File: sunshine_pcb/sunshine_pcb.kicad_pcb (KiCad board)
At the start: 2 copper layers, 82.5 x 61.9 mm, 17 parts, among them J1 XT30PW, J2 XT30PW, J3 MR30, J4 MR30, J5 USB_C_Receptacle_USB2.0_16P, SW1 Fingertech, U1 RP2350_60QFN, U2 W25Q128JVP, U3 LIS3MDL, U4 ADXL375, U5 HT7533, U6 FS2A, U7 DualAM32

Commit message: Do layout
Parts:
- added C10: 100nF, PCM_JLCPCB:C_0402, B.Cu at (104.0, 118.0)
- added C11: 100nF, PCM_JLCPCB:C_0402, B.Cu at (115.5, 116.7)
- added C12: 4.7uF, PCM_JLCPCB:C_0402, B.Cu at (109.8, 112.2)
- added C13: 100nF, PCM_JLCPCB:C_0402, B.Cu at (115.5, 120.2)
- added C14: 100nF, PCM_JLCPCB:C_0402, B.Cu at (115.5, 115.8)
- added C15: 100nF, PCM_JLCPCB:C_0402, B.Cu at (112.4, 112.2)
- added C16: 100nF, PCM_JLCPCB:C_0402, B.Cu at (108.1, 112.0)
- added C17: 100nF, PCM_JLCPCB:C_0402, B.Cu at (104.0, 116.0)
- added C18: 100nF, PCM_JLCPCB:C_0402, B.Cu at (103.9, 120.5)
- added C19: 100nF, PCM_JLCPCB:C_0402, B.Cu at (107.7, 124.2)
- added C22: 100nF, PCM_JLCPCB:C_0402, F.Cu at (112.4, 124.4)
- added C23: 15pF, PCM_JLCPCB:C_0402, B.Cu at (105.2, 109.5)
- added C24: 15pF, PCM_JLCPCB:C_0402, B.Cu at (108.2, 105.8)
- added C25: 100nF, PCM_JLCPCB:C_0402, F.Cu at (102.5, 113.3)
- added C26: 100nF, PCM_JLCPCB:C_0402, F.Cu at (98.0, 114.0)
- added C27: 100nF, PCM_JLCPCB:C_0402, F.Cu at (108.4, 109.5)
- added C28: 100nF, PCM_JLCPCB:C_0402, F.Cu at (109.8, 109.0)
- added C29: 4.7uF, PCM_JLCPCB:C_0402, F.Cu at (109.8, 109.8)
- added C3: 10u, Capacitor_SMD:C_1210_3225Metric, F.Cu at (94.8, 93.8)
- added C30: 100nF, PCM_JLCPCB:C_0402, B.Cu at (115.5, 117.5)
- added C4: 10u, Capacitor_SMD:C_1210_3225Metric, F.Cu at (101.4, 93.8)
- added C5: 10uF, PCM_JLCPCB:C_0805, F.Cu at (89.3, 126.4)
- added C6: 10uF, PCM_JLCPCB:C_0805, F.Cu at (86.2, 122.0)
- added C7: 4.7uF, PCM_JLCPCB:C_0402, B.Cu at (113.3, 123.0)
- added C8: 4.7uF, PCM_JLCPCB:C_0402, B.Cu at (111.4, 122.2)
- added C9: 4.7uF, PCM_JLCPCB:C_0402, B.Cu at (111.4, 123.0)
- added D2: 1N5819WS, PCM_JLCPCB:D_SOD-323, F.Cu at (106.6, 93.2)
- added D3: 1N5819WS, PCM_JLCPCB:D_SOD-323, F.Cu at (101.5, 117.3)
- added D4: LED, LED_SMD:LED_PLCC_2835, B.Cu at (100.0, 122.0)
- added D5: LED, LED_SMD:LED_PLCC_2835, B.Cu at (100.0, 112.8)
- added D6: LED, LED_SMD:LED_PLCC_2835, B.Cu at (100.0, 117.4)
- added D7: SMF12A, PCM_JLCPCB:D_SOD-123FL, F.Cu at (104.3, 93.8)
- added Q1: AO3401A, PCM_JLCPCB:Q_SOT-23, F.Cu at (93.7, 126.9)
- added R1: 5.1kΩ, PCM_JLCPCB:R_0402, F.Cu at (99.2, 117.3)
- added R10: 33Ω, PCM_JLCPCB:R_0805, F.Cu at (91.5, 123.3)
- added R11: 1kΩ, PCM_JLCPCB:R_0402, F.Cu at (94.5, 123.6)
- added R12: 33Ω, PCM_JLCPCB:R_0805, F.Cu at (91.5, 121.3)
- added R13: 33Ω, PCM_JLCPCB:R_0805, F.Cu at (91.5, 117.3)
- added R14: 33Ω, PCM_JLCPCB:R_0805, F.Cu at (91.5, 119.3)
- added R15: 5.1kΩ, PCM_JLCPCB:R_0402, B.Cu at (115.5, 119.3)
- added R16: 5.1kΩ, PCM_JLCPCB:R_0402, B.Cu at (117.4, 119.3)
- added R17: 5.1kΩ, PCM_JLCPCB:R_0402, B.Cu at (115.5, 118.5)
- added R18: 1kΩ, PCM_JLCPCB:R_0402, B.Cu at (117.4, 118.5)
- added R19: 5.1kΩ, PCM_JLCPCB:R_0402, F.Cu at (94.5, 124.5)
- added R2: 5.1kΩ, PCM_JLCPCB:R_0402, F.Cu at (100.5, 125.0)
- added R3: 5.1kΩ, PCM_JLCPCB:R_0402, F.Cu at (96.2, 117.8)
- added R4: 33Ω, PCM_JLCPCB:R_0402, B.Cu at (113.3, 122.2)
- added R5: 33Ω, PCM_JLCPCB:R_0402, B.Cu at (108.6, 124.2)
- added R6: 33Ω, PCM_JLCPCB:R_0402, B.Cu at (109.5, 124.2)
- added R7: 1kΩ, PCM_JLCPCB:R_0402, B.Cu at (93.8, 117.3)
- added R8: 1kΩ, PCM_JLCPCB:R_0402, B.Cu at (109.8, 107.2)
- added R9: 1kΩ, PCM_JLCPCB:R_0402, F.Cu at (114.5, 115.8)
- added S1: TS-1187A-C-B-B, PCM_JLCPCB:SW-SMD_4P-L5.1-W5.1-P3.70-LS6.5-TL-2, B.Cu at (90.1, 120.2)
- added S2: TS-1187A-C-B-B, PCM_JLCPCB:SW-SMD_4P-L5.1-W5.1-P3.70-LS6.5-TL-2, F.Cu at (109.5, 117.2)
- added U8: USBLC6-2P6, Package_TO_SOT_SMD:SOT-666, F.Cu at (100.3, 126.6)
- added Y1: ABM8-272-T3, Crystal:Crystal_SMD_3225-4Pin_3.2x2.5mm, B.Cu at (107.5, 108.3)
- D1: moved to B.Cu
- J1, J2: value XT30PW -> Soldered; footprint Connector_AMASS:AMASS_XT30PW-M_1x02_P2.50mm_Horizontal -> Connector_Wire:SolderWire-0.5sqmm_1x02_P4.6mm_D0.9mm_OD2.1mm_Relief
- J3, J4: value MR30 -> Soldered; footprint Connector_AMASS:AMASS_MR30PW-M_1x03_P3.50mm_Horizontal -> Connector_Wire:SolderWire-0.5sqmm_1x03_P4.6mm_D0.9mm_OD2.1mm_Relief
- J5: value USB_C_Receptacle_USB2.0_16P -> VerticalUSB
- L1: value L -> 3.3u; moved to B.Cu
- U1: footprint Package_DFN_QFN:QFN-60-1EP_7x7mm_P0.4mm_EP3.4x3.4mm -> Package_DFN_QFN:QFN-60-1EP_7x7mm_P0.4mm_EP3.4x3.4mm_ThermalVias; moved to B.Cu
- moved L1 78.1 mm to (111.4, 124.5)
- moved U5 77.1 mm to (85.8, 125.5)
- moved U3 66.7 mm to (109.4, 107.2)
- moved U2 66.1 mm to (108.5, 125.9)
- moved U1 66.0 mm to (109.4, 117.3)
- moved U4 65.2 mm to (100.0, 111.0), turned to 90 degrees
- moved J1 62.7 mm to (79.0, 114.0), turned to -30 degrees
- moved C1 60.4 mm to (88.4, 94.5)
- moved C2 58.6 mm to (98.1, 93.8), turned to 90 degrees
- moved J2 50.8 mm to (121.0, 86.0), turned to 150 degrees
- moved SW1 49.3 mm to (100.0, 100.0), turned to 0 degrees
- moved J4 47.2 mm to (118.0, 113.5)
- moved U6 46.4 mm to (90.0, 108.2), turned to -90 degrees
- moved J5 43.3 mm to (100.0, 121.4)
- moved D1 36.2 mm to (100.0, 126.6), turned to -90 degrees
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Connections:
- net Net-(J5-VBUS-PadA4) renamed VBUS
- C1 pad 1: unconnected-(C1-Pad1) -> VDC
- C1 pad 2: unconnected-(C1-Pad2) -> GND
- C2 pad 1: unconnected-(C2-Pad1) -> VDC
- C2 pad 2: unconnected-(C2-Pad2) -> GND
- D1 pad 1: unconnected-(D1-K-Pad1) -> GND
- D1 pad 2: unconnected-(D1-A-Pad2) -> Net-(D1-A)
- J1 pad 1: unconnected-(J1---Pad1) -> /BATT1_+
- J1 pad 2: unconnected-(J1-+-Pad2) -> /BATT2_+
- J2 pad 1: unconnected-(J2---Pad1) -> /BATT2_+
- J2 pad 2: unconnected-(J2-+-Pad2) -> GND
- J3 pad 1: unconnected-(J3-Pin_1-Pad1) -> Net-(J3-Pin_1)
- J3 pad 2: unconnected-(J3-Pin_2-Pad2) -> Net-(J3-Pin_2)
- J3 pad 3: unconnected-(J3-Pin_3-Pad3) -> Net-(J3-Pin_3)
- J4 pad 1: unconnected-(J4-Pin_1-Pad1) -> Net-(J4-Pin_1)
- J4 pad 2: unconnected-(J4-Pin_2-Pad2) -> Net-(J4-Pin_2)
- J4 pad 3: unconnected-(J4-Pin_3-Pad3) -> Net-(J4-Pin_3)
- J5 pad A1: Net-(J5-GND-PadA1) -> GND
- J5 pad A12: Net-(J5-GND-PadA1) -> GND
- J5 pad A5: unconnected-(J5-CC1-PadA5) -> Net-(J5-CC1)
- J5 pad A6: unconnected-(J5-D+-PadA6) -> /USB_C_D+
- J5 pad A7: unconnected-(J5-D--PadA7) -> /USB_C_D-
- J5 pad B1: Net-(J5-GND-PadA1) -> GND
- J5 pad B12: Net-(J5-GND-PadA1) -> GND
- J5 pad B5: unconnected-(J5-CC2-PadB5) -> Net-(J5-CC2)
- J5 pad B6: unconnected-(J5-D+-PadB6) -> /USB_C_D+
- J5 pad B7: unconnected-(J5-D--PadB7) -> /USB_C_D-
- J5 pad S1: unconnected-(J5-SHIELD-PadS1) -> Net-(J5-SHIELD)
- L1 pad 1: unconnected-(L1-Pad1) -> +1V1
- L1 pad 2: unconnected-(L1-Pad2) -> /VREG_LX
- SW1 pad 1: unconnected-(SW1-A-Pad1) -> /BATT1_+
- SW1 pad 2: unconnected-(SW1-B-Pad2) -> VDC
- U1 pad 1: unconnected-(U1-IOVDD-Pad1) -> +3V3
- U1 pad 10: unconnected-(U1-GPIO7-Pad10) -> /R4
- U1 pad 11: unconnected-(U1-IOVDD-Pad11) -> +3V3
- U1 pad 12: unconnected-(U1-GPIO8-Pad12) -> /S2
- U1 pad 13: unconnected-(U1-GPIO9-Pad13) -> /LED
- U1 pad 14: unconnected-(U1-GPIO10-Pad14) -> /IMU_SCK
- U1 pad 15: unconnected-(U1-GPIO11-Pad15) -> /IMU_MOSI
- U1 pad 16: unconnected-(U1-GPIO12-Pad16) -> /IMU_MISO
- U1 pad 17: unconnected-(U1-GPIO13-Pad17) -> /IMU_CS
- U1 pad 18: unconnected-(U1-GPIO14-Pad18) -> /IMU_INT1
- U1 pad 19: unconnected-(U1-GPIO15-Pad19) -> /IMU_INT2
- U1 pad 20: unconnected-(U1-IOVDD-Pad20) -> +3V3
- U1 pad 21: unconnected-(U1-XIN-Pad21) -> Net-(U1-XIN)
- U1 pad 22: unconnected-(U1-XOUT-Pad22) -> Net-(U1-XOUT)
- U1 pad 23: unconnected-(U1-DVDD-Pad23) -> +1V1
- U1 pad 26: unconnected-(U1-RUN-Pad26) -> /RESET
- U1 pad 27: unconnected-(U1-GPIO16-Pad27) -> /MAG_MISO
- U1 pad 28: unconnected-(U1-GPIO17-Pad28) -> /MAG_CS
- U1 pad 29: unconnected-(U1-GPIO18-Pad29) -> /MAG_SCK
- U1 pad 3: unconnected-(U1-GPIO1-Pad3) -> /R1
- U1 pad 30: unconnected-(U1-IOVDD-Pad30) -> +3V3
- U1 pad 31: unconnected-(U1-GPIO19-Pad31) -> /MAG_MOSI
- U1 pad 32: unconnected-(U1-GPIO20-Pad32) -> /MAG_DRDY
- U1 pad 33: unconnected-(U1-GPIO21-Pad33) -> /MAG_INT
- U1 pad 38: unconnected-(U1-IOVDD-Pad38) -> +3V3
- U1 pad 39: unconnected-(U1-DVDD-Pad39) -> +1V1
- U1 pad 40: unconnected-(U1-GPIO26_ADC0-Pad40) -> Net-(U1-GPIO26_ADC0)
- U1 pad 44: unconnected-(U1-ADC_AVDD-Pad44) -> +3V3
- U1 pad 45: unconnected-(U1-IOVDD-Pad45) -> +3V3
- U1 pad 46: unconnected-(U1-VREG_AVDD-Pad46) -> /VREG_AVDD
- U1 pad 47: unconnected-(U1-VREG_PGND-Pad47) -> GND
- U1 pad 48: unconnected-(U1-VREG_LX-Pad48) -> /VREG_LX
- U1 pad 49: unconnected-(U1-VREG_VIN-Pad49) -> +3V3
- U1 pad 5: unconnected-(U1-GPIO3-Pad5) -> /R2
- U1 pad 50: unconnected-(U1-VREG_FB-Pad50) -> +1V1
- U1 pad 51: unconnected-(U1-USB_DM-Pad51) -> Net-(U1-USB_DM)
- U1 pad 52: unconnected-(U1-USB_DP-Pad52) -> Net-(U1-USB_DP)
- U1 pad 53: unconnected-(U1-USB_OTP_VDD-Pad53) -> +3V3
- U1 pad 54: unconnected-(U1-QSPI_IOVDD-Pad54) -> +3V3
- U1 pad 55: unconnected-(U1-QSPI_SD3-Pad55) -> /QSPI_SD3
- U1 pad 56: unconnected-(U1-QSPI_SCLK-Pad56) -> /QSPI_SCK
- U1 pad 57: unconnected-(U1-QSPI_SD0-Pad57) -> /QSPI_SD0
- U1 pad 58: unconnected-(U1-QSPI_SD2-Pad58) -> /QSPI_SD2
- U1 pad 59: unconnected-(U1-QSPI_SD1-Pad59) -> /QSPI_SD1
- U1 pad 6: unconnected-(U1-DVDD-Pad6) -> +1V1
- U1 pad 60: unconnected-(U1-QSPI_SS-Pad60) -> /QSPI_SS
- U1 pad 61: unconnected-(U1-GND-Pad61) -> GND
- U1 pad 8: unconnected-(U1-GPIO5-Pad8) -> /R3
- U1 pad 9: unconnected-(U1-GPIO6-Pad9) -> /S1
- U2 pad 1: unconnected-(U2-~{CS}-Pad1) -> /QSPI_SS
- U2 pad 2: unconnected-(U2-DO/IO_{1}-Pad2) -> /QSPI_SD1
- U2 pad 3: unconnected-(U2-~{WP}/IO_{2}-Pad3) -> /QSPI_SD2
- U2 pad 4: unconnected-(U2-GND-Pad4) -> GND
- U2 pad 5: unconnected-(U2-DI/IO_{0}-Pad5) -> /QSPI_SD0
- U2 pad 6: unconnected-(U2-CLK-Pad6) -> /QSPI_SCK
- U2 pad 7: unconnected-(U2-~{HOLD}/~{RESET}/IO_{3}-Pad7) -> /QSPI_SD3
- U2 pad 8: unconnected-(U2-VCC-Pad8) -> +3V3
- U2 pad 9: unconnected-(U2-EP-Pad9) -> GND
- U3 pad 1: unconnected-(U3-SCL/SPC-Pad1) -> /MAG_SCK
- U3 pad 10: unconnected-(U3-~{CS}-Pad10) -> /MAG_CS
- U3 pad 11: unconnected-(U3-SDA/SDI/SDO-Pad11) -> /MAG_MOSI
- U3 pad 12: Net-(U3-GND-Pad12) -> GND
- U3 pad 2: Net-(U3-GND-Pad12) -> GND
- U3 pad 3: Net-(U3-GND-Pad12) -> GND
- U3 pad 4: unconnected-(U3-C1-Pad4) -> Net-(U3-C1)
- U3 pad 5: unconnected-(U3-Vdd-Pad5) -> +3V3
- U3 pad 6: unconnected-(U3-Vdd_IO-Pad6) -> +3V3
- U3 pad 7: unconnected-(U3-INT-Pad7) -> /MAG_INT
- U3 pad 8: unconnected-(U3-DRDY-Pad8) -> /MAG_DRDY
- U3 pad 9: unconnected-(U3-SDO/SA1-Pad9) -> /MAG_MISO
- U4 pad 1: unconnected-(U4-Vdd_I/O-Pad1) -> +3V3
- U4 pad 12: unconnected-(U4-SDO/ADDR-Pad12) -> /IMU_MISO
- U4 pad 13: unconnected-(U4-SDA/SDI/SDIO-Pad13) -> /IMU_MOSI
- U4 pad 14: unconnected-(U4-SCL/SCLK-Pad14) -> /IMU_SCK
- U4 pad 2: Net-(U4-GND-Pad2) -> GND
- U4 pad 4: Net-(U4-GND-Pad2) -> GND
- U4 pad 5: Net-(U4-GND-Pad2) -> GND
- U4 pad 6: unconnected-(U4-Vs-Pad6) -> +3V3
- U4 pad 7: unconnected-(U4-~{CS}-Pad7) -> /IMU_CS
- U4 pad 8: unconnected-(U4-INT1-Pad8) -> /IMU_INT1
- U4 pad 9: unconnected-(U4-INT2-Pad9) -> /IMU_INT2
- U5 pad 1: unconnected-(U5-GND-Pad1) -> GND
- U5 pad 2: unconnected-(U5-VIN-Pad2) -> +5V
- U5 pad 3: unconnected-(U5-VOUT-Pad3) -> +3V3
- U6 pad 1: unconnected-(U6-Pad1) -> /R1
- U6 pad 2: unconnected-(U6-Pad2) -> /R2
- U6 pad 3: unconnected-(U6-Pad3) -> /R3
- U6 pad 4: unconnected-(U6-Pad4) -> /R4
- U6 pad 5: unconnected-(U6-+5V-Pad5) -> +5V
- U6 pad 6: unconnected-(U6-GND-Pad6) -> GND
- U7 pad 1: unconnected-(U7-M1A-Pad1) -> Net-(J3-Pin_3)
- U7 pad 10: unconnected-(U7-S2-Pad10) -> /S2
- U7 pad 11: unconnected-(U7-+5V-Pad11) -> Net-(U7-+5V)
- U7 pad 12: Net-(U7-GND-Pad12) -> GND
- U7 pad 2: unconnected-(U7-M1B-Pad2) -> Net-(J3-Pin_2)
- U7 pad 3: unconnected-(U7-M1C-Pad3) -> Net-(J3-Pin_1)
- U7 pad 4: unconnected-(U7-M2A-Pad4) -> Net-(J4-Pin_1)
- U7 pad 5: unconnected-(U7-M2B-Pad5) -> Net-(J4-Pin_2)
- U7 pad 6: unconnected-(U7-M2C-Pad6) -> Net-(J4-Pin_3)
- U7 pad 7: unconnected-(U7-+VDC-Pad7) -> VDC
- U7 pad 8: Net-(U7-GND-Pad12) -> GND
- U7 pad 9: unconnected-(U7-S1-Pad9) -> /S1
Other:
- board size 82.5 x 61.9 mm -> 59 x 58 mm
- board text added: "+"

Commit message: Add some protection
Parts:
- added D10: SMF5.0A, PCM_JLCPCB:D_SOD-123FL, F.Cu at (113.5, 93.7)
- added D8: SMF5.0A, PCM_JLCPCB:D_SOD-123FL, F.Cu at (108.7, 93.7)
- added D9: SMF5.0A, PCM_JLCPCB:D_SOD-123FL, F.Cu at (111.1, 93.7)
- added R20: 1kΩ, PCM_JLCPCB:R_0402, F.Cu at (106.5, 95.1)
- added R21: 1kΩ, PCM_JLCPCB:R_0402, F.Cu at (106.5, 96.0)
- J1, J2: footprint Connector_Wire:SolderWire-0.5sqmm_1x02_P4.6mm_D0.9mm_OD2.1mm_Relief -> Connector_Wire:SolderWire-0.75sqmm_1x02_P4.8mm_D1.25mm_OD2.3mm_Relief
- moved J1 1.58 mm to (79.5, 112.5)
- moved J2 1.58 mm to (120.5, 87.5)
- moved D2 0.22 mm to (106.5, 93.0), turned to 90 degrees
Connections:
- U7 pad 10: /S2 -> /S2_C
- U7 pad 9: /S1 -> /S1_C

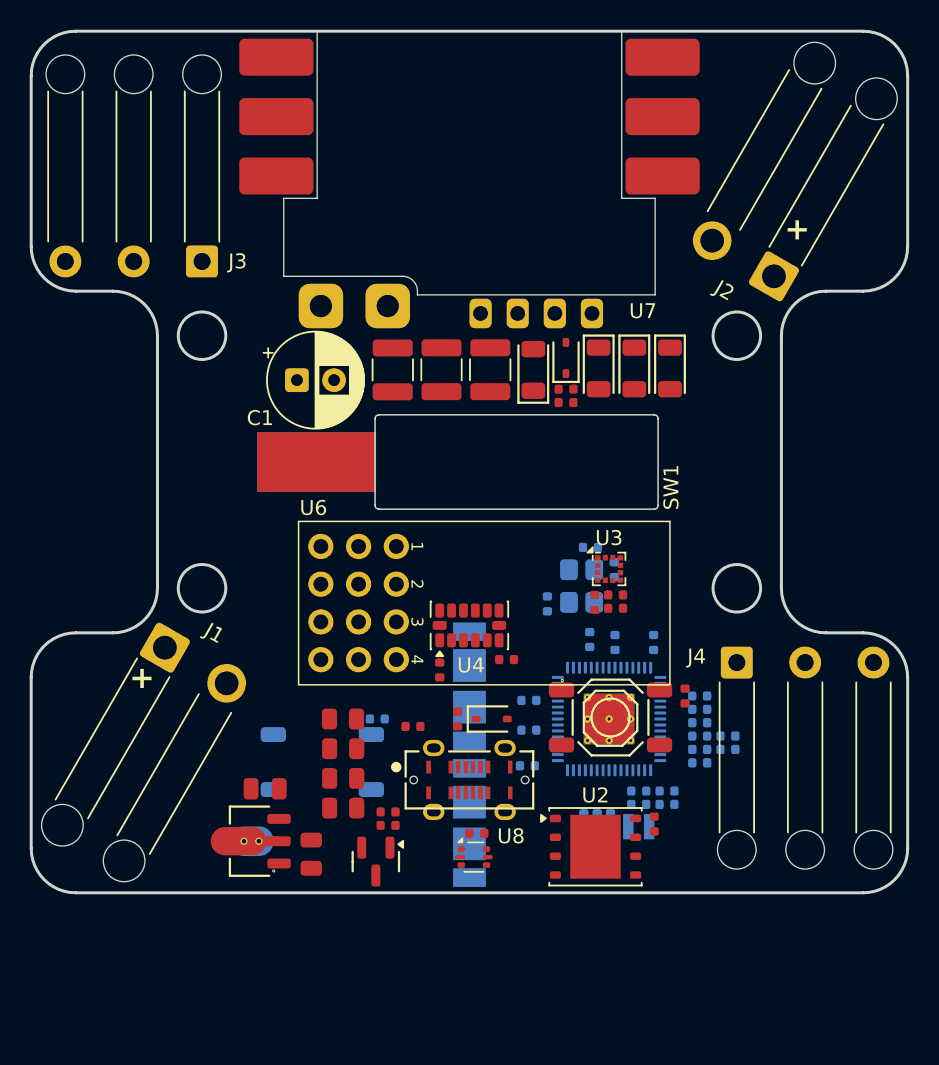
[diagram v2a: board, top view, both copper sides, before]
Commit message: Re-layout board for ESP32
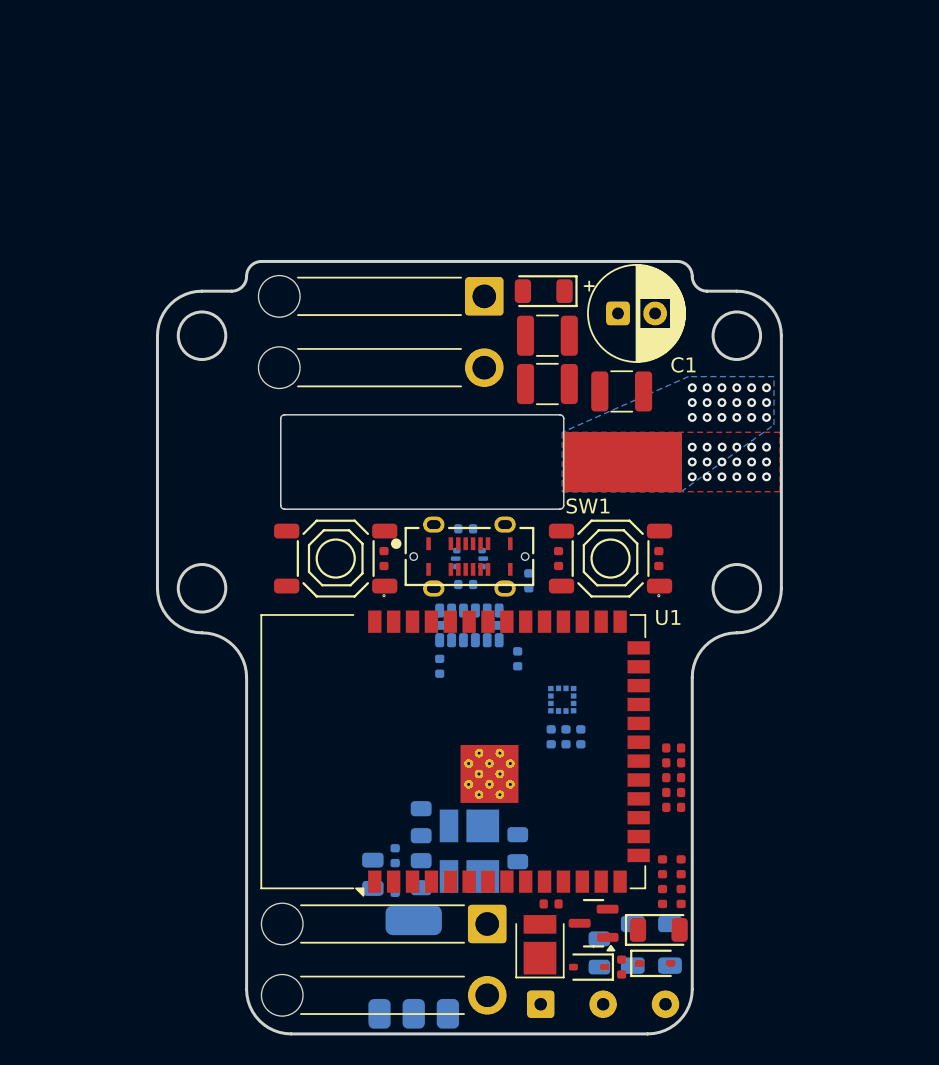
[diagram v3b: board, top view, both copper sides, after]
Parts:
- removed C10, C11, C13, C14, C15, C16, C17, C18, C19, C22: 100nF, PCM_JLCPCB:C_0402
- removed C12: 4.7uF, PCM_JLCPCB:C_0402
- removed C23, C24: 15pF, PCM_JLCPCB:C_0402
- removed D6: LED, LED_SMD:LED_PLCC_2835
- removed J4: Soldered, Connector_Wire:SolderWire-0.5sqmm_1x03_P4.6mm_D0.9mm_OD2.1mm_Relief
- removed L1: 3.3u, custom:L_pol_2016
- removed R14: 33Ω, PCM_JLCPCB:R_0805
- removed R8, R9: 1kΩ, PCM_JLCPCB:R_0402
- removed U5: HT7533, PCM_JLCPCB:SOT-89-3_L4.5-W2.5-P1.50-LS4.2-BR
- removed U6: FS2A, custom:FS2A
- removed U7: DualAM32, custom:DualAM32
- removed Y1: ABM8-272-T3, Crystal:Crystal_SMD_3225-4Pin_3.2x2.5mm
- C25, C26, C27, C28, C29, C5, C6, D10, D9, R1, R10, R12, R13, R2, R3, U3, U4, U8: moved to B.Cu
- C30, D5, R15, R16, R17, R18: moved to F.Cu
- C7: value 4.7uF -> 100nF; moved to F.Cu
- C9: value 4.7uF -> 100nF
- J2: value Soldered -> Conn_01x03; footprint Connector_Wire:SolderWire-0.75sqmm_1x02_P4.8mm_D1.25mm_OD2.3mm_Relief -> Connector_Wire:SolderWire-0.25sqmm_1x03_P4.2mm_D0.65mm_OD1.7mm
- J3: footprint Connector_Wire:SolderWire-0.5sqmm_1x03_P4.6mm_D0.9mm_OD2.1mm_Relief -> Connector_Wire:SolderWire-0.75sqmm_1x02_P4.8mm_D1.25mm_OD2.3mm_Relief
- R4, R5, R6: value 33Ω -> 5.1kΩ; moved to F.Cu
- R7: value 1kΩ -> 5.1kΩ; moved to F.Cu
- S1: value TS-1187A-C-B-B -> TS-1187A-C-C-B; moved to F.Cu
- S2: value TS-1187A-C-B-B -> TS-1187A-C-C-B
- U1: value RP2350_60QFN -> ESP32-S3-WROOM-1; footprint Package_DFN_QFN:QFN-60-1EP_7x7mm_P0.4mm_EP3.4x3.4mm_ThermalVias -> RF_Module:ESP32-S3-WROOM-1; moved to F.Cu
- U2: value W25Q128JVP -> SPX1117M3; footprint Package_SON:WSON-8-1EP_6x5mm_P1.27mm_EP3.4x4.3mm -> Package_TO_SOT_SMD:SOT-223-3_TabPin2; moved to B.Cu
- moved J2 51.5 mm to (104.8, 136.5), turned to 0 degrees
- moved J3 48.6 mm to (101.2, 131.1), turned to -90 degrees
- moved D2 41.0 mm to (108.0, 134.0), turned to 180 degrees
- moved D10 38.9 mm to (111.0, 132.5), turned to 90 degrees
- moved D9 38.9 mm to (113.5, 132.5), turned to 90 degrees
- moved D8 38.0 mm to (112.8, 131.5), turned to 0 degrees
- moved R20 35.0 mm to (114.2, 129.2), turned to -90 degrees
- moved R21 33.9 mm to (113.0, 129.2), turned to -90 degrees
- moved J1 32.0 mm to (101.0, 88.8), turned to -90 degrees
- moved S1 23.7 mm to (109.5, 106.5)
- moved R5 22.7 mm to (94.2, 106.5)
- moved C1 22.1 mm to (110.0, 90.0)
- moved R7 21.6 mm to (113.0, 127.2), turned to -90 degrees
- moved S2 21.4 mm to (91.0, 106.5), turned to 180 degrees
- moved C5 20.5 mm to (108.8, 133.1), turned to 90 degrees
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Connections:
- C30 pad 1: Net-(U1-GPIO26_ADC0) -> /VBUS_DIV
- C7 pad 1: /VREG_AVDD -> /EN
- C9 pad 1: +1V1 -> +3V3
- D2 pad 2: Net-(U7-+5V) -> /5V_IN
- J1 pad 2: /BATT2_+ -> GND
- J2 pad 1: /BATT2_+ -> /5V_IN
- J2 pad 2: GND -> /S1_C
- J3 pad 1: Net-(J3-Pin_1) -> VDC
- J3 pad 2: Net-(J3-Pin_2) -> GND
- R15 pad 2: Net-(U1-GPIO26_ADC0) -> /VBUS_DIV
- R17 pad 1: Net-(U1-GPIO26_ADC0) -> /VBUS_DIV
- R4 pad 2: /VREG_AVDD -> /EN
- R5 pad 1: Net-(U1-USB_DP) -> +3V3
- R5 pad 2: /USB_D+ -> /BOOT
- R6 pad 1: Net-(U1-USB_DM) -> +3V3
- R6 pad 2: /USB_D- -> /S1
- R7 pad 1: /QSPI_SS -> +3V3
- R7 pad 2: Net-(S1-A) -> /S2
- S1 pad 1: Net-(S1-A) -> /EN
- S1 pad 2: Net-(S1-A) -> /EN
- S2 pad 1: Net-(S2-A) -> /BOOT
- S2 pad 2: Net-(S2-A) -> unconnected-(S2-B-Pad2)
- S2 pad 4: GND -> unconnected-(S2-D-Pad4)
- SW1 pad 1: /BATT1_+ -> VDC
- SW1 pad 2: VDC -> /BATT1_+
- U1 pad 1: +3V3 -> GND
- U1 pad 10: /R4 -> /MAG_MISO
- U1 pad 11: +3V3 -> /MAG_CS
- U1 pad 12: /S2 -> /IMU_INT1
- U1 pad 13: /LED -> /USB_D-
- U1 pad 14: /IMU_SCK -> /USB_D+
- U1 pad 15: /IMU_MOSI -> unconnected-(U1-IO3-Pad15)
- U1 pad 16: /IMU_MISO -> unconnected-(U1-IO46-Pad16)
- U1 pad 17: /IMU_CS -> /IMU_INT2
- U1 pad 18: /IMU_INT1 -> /IMU_CS
- U1 pad 19: /IMU_INT2 -> /IMU_MOSI
- U1 pad 2: unconnected-(U1-GPIO0-Pad2) -> +3V3
- U1 pad 20: +3V3 -> /IMU_SCK
- U1 pad 21: Net-(U1-XIN) -> /IMU_MISO
- U1 pad 22: Net-(U1-XOUT) -> /MAG_DRDY
- U1 pad 23: +1V1 -> /MAG_INT
- U1 pad 26: /RESET -> unconnected-(U1-IO45-Pad26)
- U1 pad 27: /MAG_MISO -> /BOOT
- U1 pad 28: /MAG_CS -> unconnected-(U1-IO35-Pad28)
- U1 pad 29: /MAG_SCK -> unconnected-(U1-IO36-Pad29)
- U1 pad 3: /R1 -> /EN
- U1 pad 30: +3V3 -> unconnected-(U1-IO37-Pad30)
- U1 pad 31: /MAG_MOSI -> /LED
- U1 pad 32: /MAG_DRDY -> unconnected-(U1-IO39-Pad32)
- U1 pad 33: /MAG_INT -> unconnected-(U1-IO40-Pad33)
- U1 pad 38: +3V3 -> unconnected-(U1-IO2-Pad38)
- U1 pad 39: +1V1 -> unconnected-(U1-IO1-Pad39)
- U1 pad 4: unconnected-(U1-GPIO2-Pad4) -> /S1
- U1 pad 40: Net-(U1-GPIO26_ADC0) -> GND
- U1 pad 41: unconnected-(U1-GPIO27_ADC1-Pad41) -> GND
- U1 pad 5: /R2 -> /S2
- U1 pad 6: +1V1 -> unconnected-(U1-IO6-Pad6)
- U1 pad 7: unconnected-(U1-GPIO4-Pad7) -> /VBUS_DIV
- U1 pad 8: /R3 -> /MAG_MOSI
- U1 pad 9: /S1 -> /MAG_SCK
- U2 pad 1: /QSPI_SS -> GND
- U2 pad 2: /QSPI_SD1 -> +3V3
- U2 pad 3: /QSPI_SD2 -> +5V
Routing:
- net VDC: vias 0 -> 18
- net /BATT1_+: vias 0 -> 18
- added copper zone on B.Cu, net /BATT1_+
- added copper zone on In2.Cu, net /BATT1_+
- added copper zone on In1.Cu, net GND
- added copper zone on F.Cu, net VDC
- added copper zone on In2.Cu, net VDC
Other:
- board size 59 x 58 mm -> 42 x 52 mm
- copper layers 2 -> 4
- board text removed: "+"

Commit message: Fix issue with mosfet
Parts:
- removed R19: 5.1kΩ, PCM_JLCPCB:R_0402
- Q1: value AO3401A -> AO3400A
- moved Q1 0.28 mm to (108.6, 131.2), turned to 0 degrees
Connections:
- D1 pad 1: GND -> Net-(D1-K)
- D4 pad 1: GND -> Net-(D1-K)
- D5 pad 1: GND -> Net-(D1-K)
- Q1 pad 2: +5V -> GND
- Q1 pad 3: Net-(Q1-D) -> Net-(D1-K)
- R10 pad 1: Net-(Q1-D) -> +5V
- R12 pad 1: Net-(Q1-D) -> +5V
- R13 pad 1: Net-(Q1-D) -> +5V

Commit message: Route PCB
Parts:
- moved U8 9.40 mm to (109.4, 106.5), turned to 0 degrees
- moved C29 4.30 mm to (108.0, 115.0), turned to 90 degrees
- moved C27 3.81 mm to (106.0, 115.0), turned to 90 degrees
- moved C25 3.72 mm to (96.8, 110.2)
- moved C28 3.54 mm to (107.0, 115.0), turned to 90 degrees
- moved C26 3.00 mm to (103.2, 110.2), turned to 90 degrees
- moved U3 1.80 mm to (107.2, 117.5), turned to 0 degrees
- moved R2 1.00 mm to (100.8, 108.2), turned to 180 degrees
- moved R1 0.50 mm to (99.2, 104.5), turned to 180 degrees
- moved R3 0.25 mm to (104.0, 108.2), turned to 90 degrees
- turned U4 to -90 degrees
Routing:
- net +3V3: track 0.00 -> 110.2 mm, vias 0 -> 12
- net VBUS: track 0.00 -> 74.4 mm, vias 0 -> 3
- net GND: track 0.00 -> 59.3 mm, vias 0 -> 29
- net +5V: track 0.00 -> 56.5 mm, vias 0 -> 1
- net /EN: track 0.00 -> 38.1 mm, vias 0 -> 2
- net /USB_D+: track 0.00 -> 26.0 mm, vias 0 -> 1
- net /IMU_SCK: track 0.00 -> 25.7 mm, vias 0 -> 1
- net /IMU_MOSI: track 0.00 -> 25.0 mm, vias 0 -> 1
- net /USB_D-: track 0.00 -> 24.9 mm, vias 0 -> 1
- net /USB_C_D+: track 0.00 -> 24.7 mm, vias 0 -> 3
- net /VBUS_DIV: track 0.00 -> 24.7 mm, vias 0 -> 2
- net /BOOT: track 0.00 -> 23.8 mm, vias 0 -> 2
- net /IMU_INT2: track 0.00 -> 23.3 mm, vias 0 -> 1
- net /S1: track 0.00 -> 23.2 mm, vias 0 -> 2
- net Net-(J5-SHIELD): track 0.00 -> 22.9 mm, vias 0 -> 1
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- added copper zone on B.Cu, net GND
- added copper zone on F.Cu, net GND
